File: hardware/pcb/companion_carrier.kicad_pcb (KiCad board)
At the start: 2 copper layers, 44 x 104 mm, 17 parts

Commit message: SW6 resolved: C&K OS102011MA1QN1 side-exit THT slide [LOCKED]
Geoff initially picked the CIT ANT11SF1CQE toggle from the issue #16
survey, but its perpendicular-to-PCB mounting forced a raised front-face
turret in the enclosure -- rejected on render preview as unworkable.
Reverted same day to the survey's original leading candidate, the C&K
OS102011MA1QN1: right-angle THT slide, same side-exit concept as the
original PCM12 design, so the shell returns to its flat 22.6mm form.

Real datasheet dimensions (OS series p. I-42, fetched via LCSC):
body 8.6 x 3.9 x 4.4mm -- fits under the existing 5.5mm front-wall
clearance with no enclosure change. 3 PC pins (0.8mm, 2.1mm pitch) + 2
support legs (1.5mm, 8.2mm span) encoded in a new slide_os102() THT
footprint replacing the SMT slide_pcm12(). In LCSC catalog (C226259),
so JLCPCB can place it in standard PCBA -- no consignment needed.

PCB/enclosure/mockup regenerated; toggle constants and turret removed.

Co-Authored-By: Claude Sonnet 5 <noreply@anthropic.com>
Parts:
- SW6: footprint carrier:CK_PCM12SMTR -> carrier:CK_OS102011MA1QN1
- moved SW6 0.15 mm to (80.0, 46.0)
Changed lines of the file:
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@@
       (net 1 "GND"))
   )
-  (footprint "carrier:CK_PCM12SMTR" (version 20240108) (generator generate_pcb.py) (layer "F.Cu")
-    (at 80.2 46.0)
-    (attr smd)
+  (footprint "carrier:CK_OS102011MA1QN1" (version 20240108) (generator generate_pcb.py) (layer "F.Cu")
+    (at 80.05 46.0)
+    (attr through_hole)
     (fp_text reference "SW6" (at 0 -3.0) (layer "F.SilkS")
       (effects (font (size 0.8 0.8) (thickness 0.12)))
     )
-    (fp_line (start -1.8 -4.35) (end 1.8 -4.35) (layer "F.SilkS") (width 0.12))
-    (fp_line (start 1.8 -4.35) (end 1.8 4.35) (layer "F.SilkS") (width 0.12))
-    (fp_line (start 1.8 4.35) (end -1.8 4.35) (layer "F.SilkS") (width 0.12))
-    (fp_line (start -1.8 4.35) (end -1.8 -4.35) (layer "F.SilkS") (width 0.12))
-    (pad "1" smd roundrect (at -2.4 -2.5) (size 1.6 1.0) (layers "F.Cu" "F.Mask" "F.Paste") (roundrect_rratio 0.25)
+    (fp_line (start -1.95 -4.3) (end 1.95 -4.3) (layer "F.SilkS") (width 0.12))
+    (fp_line (start 1.95 -4.3) (end 1.95 4.3) (layer "F.SilkS") (width 0.12))
+    (fp_line (start 1.95 4.3) (end -1.95 4.3) (layer "F.SilkS") (width 0.12))
+    (fp_line (start -1.95 4.3) (end -1.95 -4.3) (layer "F.SilkS") (width 0.12))
+    (pad "1" thru_hole circle (at -1.0 -2.1) (size 1.6 1.6) (drill 0.8) (layers *.Cu *.Mask)
       (net 5 "LATCH"))
-    (pad "2" smd roundrect (at -2.4 0.0) (size 1.6 1.0) (layers "F.Cu" "F.Mask" "F.Paste") (roundrect_rratio 0.25)
+    (pad "2" thru_hole circle (at -1.0 0.0) (size 1.6 1.6) (drill 0.8) (layers *.Cu *.Mask)
       (net 1 "GND"))
-    (pad "3" smd roundrect (at -2.4 2.5) (size 1.6 1.0) (layers "F.Cu" "F.Mask" "F.Paste") (roundrect_rratio 0.25))
-    (pad "MP1" smd roundrect (at 1.2 -3.6) (size 1.8 1.4) (layers "F.Cu" "F.Mask" "F.Paste") (roundrect_rratio 0.25))
-    (pad "MP2" smd roundrect (at 1.2 3.6) (size 1.8 1.4) (layers "F.Cu" "F.Mask" "F.Paste") (roundrect_rratio 0.25))
+    (pad "3" thru_hole circle (at -1.0 2.1) (size 1.6 1.6) (drill 0.8) (layers *.Cu *.Mask))
+    (pad "MP1" thru_hole circle (at 0.5 -4.1) (size 2.4 2.4) (drill 1.5) (layers *.Cu *.Mask))
+    (pad "MP2" thru_hole circle (at 0.5 4.1) (size 2.4 2.4) (drill 1.5) (layers *.Cu *.Mask))
   )
   (footprint "carrier:MicBreakout_SPH0645-style" (version 20240108) (generator generate_pcb.py) (layer "F.Cu")

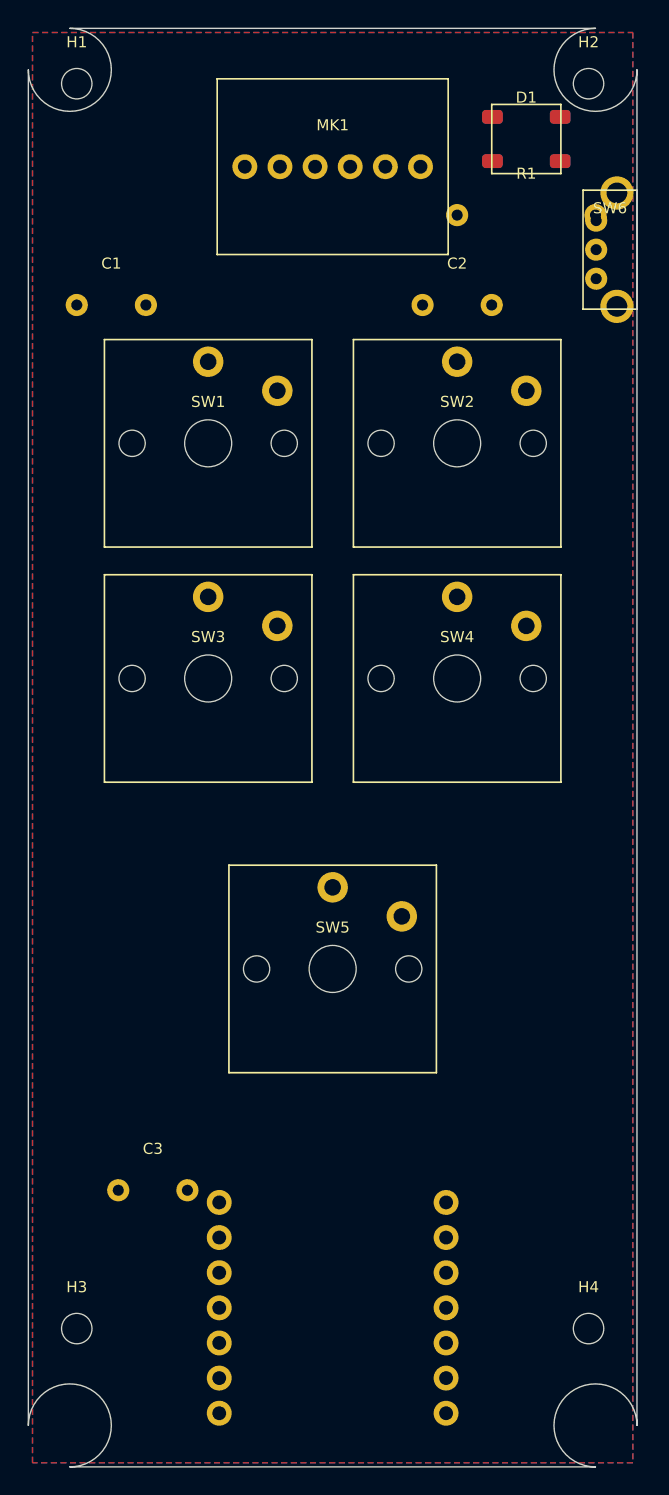
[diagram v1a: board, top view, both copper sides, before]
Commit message: Route carrier board: DRC-clean, fab package exported (v0)
Fab-ready pass, run entirely headless: KiCad 10.0.4 installed to
user-space (~/Applications, drag-drop DMG -- no sudo) + freerouting
2.2.4. New hardware/pcb/route_board.py makes the routing reproducible:
generate_pcb.py -> Specctra DSN -> freerouting -> SES import -> zone
fill, then kicad-cli DRC.

The first real DRC run caught two genuine placement bugs, both fixed in
the generator: R1's +X pad landed exactly on SW6 pin 1 (the OS102011 THT
pin row reaches further into the board than the old PCM12 SMT pads --
moved R1 to x=8), and SW6's support-leg pads sat 0.25mm from the board
edge (moved to the footprint centreline). SW5's GND pad now uses a solid
zone connection: the PTT switch's stem/post holes crowd the F.Cu zone
below the 2-spoke thermal-relief minimum, and a stitch track only
reached an isolated island.

Final DRC: 0 error-severity violations, 0 unconnected items.

Front silkscreen: "agent-ptt-mic-v0 / Geoff Dudgeon & Claude" per
Geoff's request, placed in the clear band between PTT and the XIAO pin
field.

fab/ contains Gerbers + Excellon drill (zip is JLCPCB/PCBWay
upload-ready), CPL/pos CSV for assembly quoting, and 3D renders of the
routed board. No fab order placed -- quoting next, order needs Geoff's
explicit go-ahead per the standing rule.

Co-Authored-By: Claude Sonnet 5 <noreply@anthropic.com>
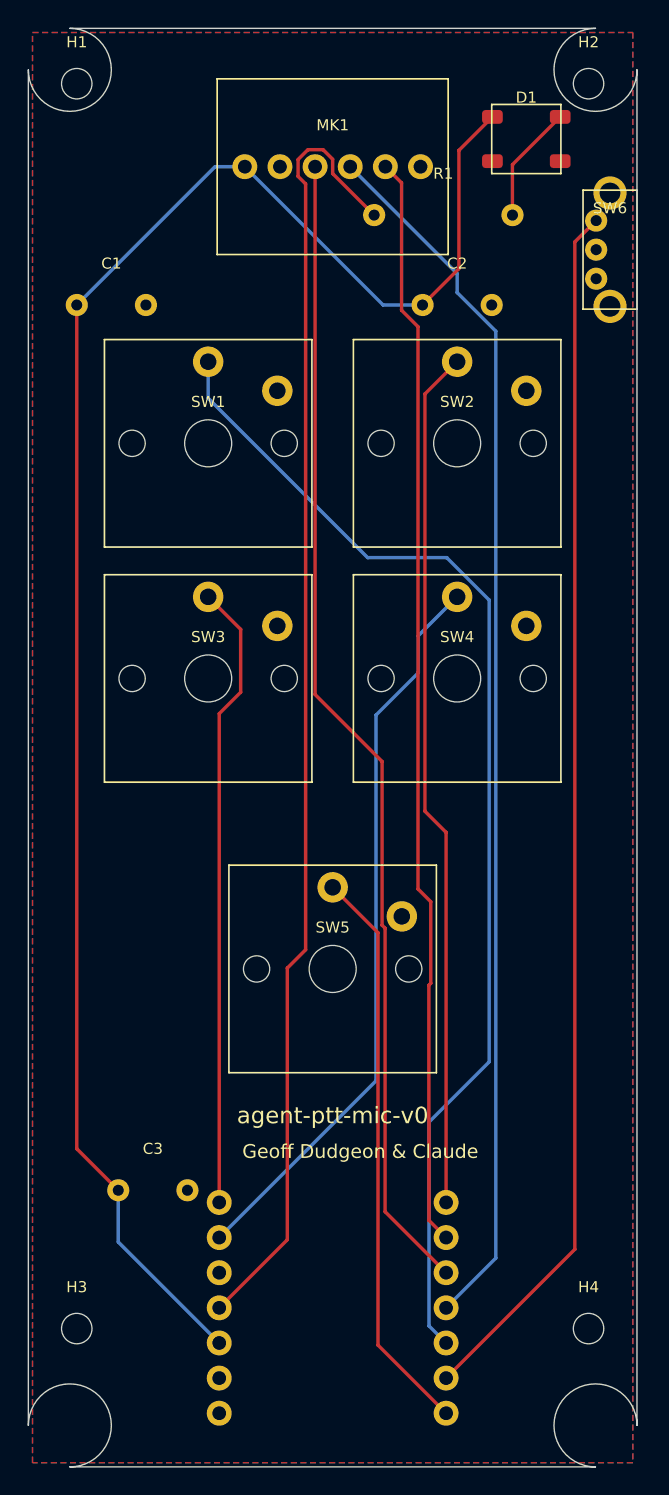
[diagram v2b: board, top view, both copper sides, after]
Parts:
- moved R1 6.00 mm to (68.0, 43.5)
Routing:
- net 3V3: track 0.00 -> 128.3 mm
- net LED_DATA: track 0.00 -> 94.2 mm
- net I2S_SD: track 0.00 -> 88.3 mm
- net LATCH: track 0.00 -> 88.2 mm
- net KEY_APPROVE: track 0.00 -> 85.0 mm
- net I2S_BCLK: track 0.00 -> 83.9 mm
- net I2S_LRCLK: track 0.00 -> 79.4 mm
- net KEY_REMEMBER: track 0.00 -> 62.4 mm
- net KEY_MODE: track 0.00 -> 53.4 mm
- net KEY_REJECT: track 0.00 -> 45.4 mm
- net PTT: track 0.00 -> 41.4 mm
- net LED_DIN: track 0.00 -> 8.53 mm
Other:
- rule pad_to_mask_clearance: 0.0 -> 0
- board text added: "Geoff Dudgeon & Claude"
- board text added: "agent-ptt-mic-v0"
